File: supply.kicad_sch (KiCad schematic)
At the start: 71 parts, among them Q6 DMG1012T-7, U4 TPS2117DRLR, U5 TPS2117DRLR, U6 PAC1934T_WLCSP, U7 MP5424GRM, U8 MP8869S

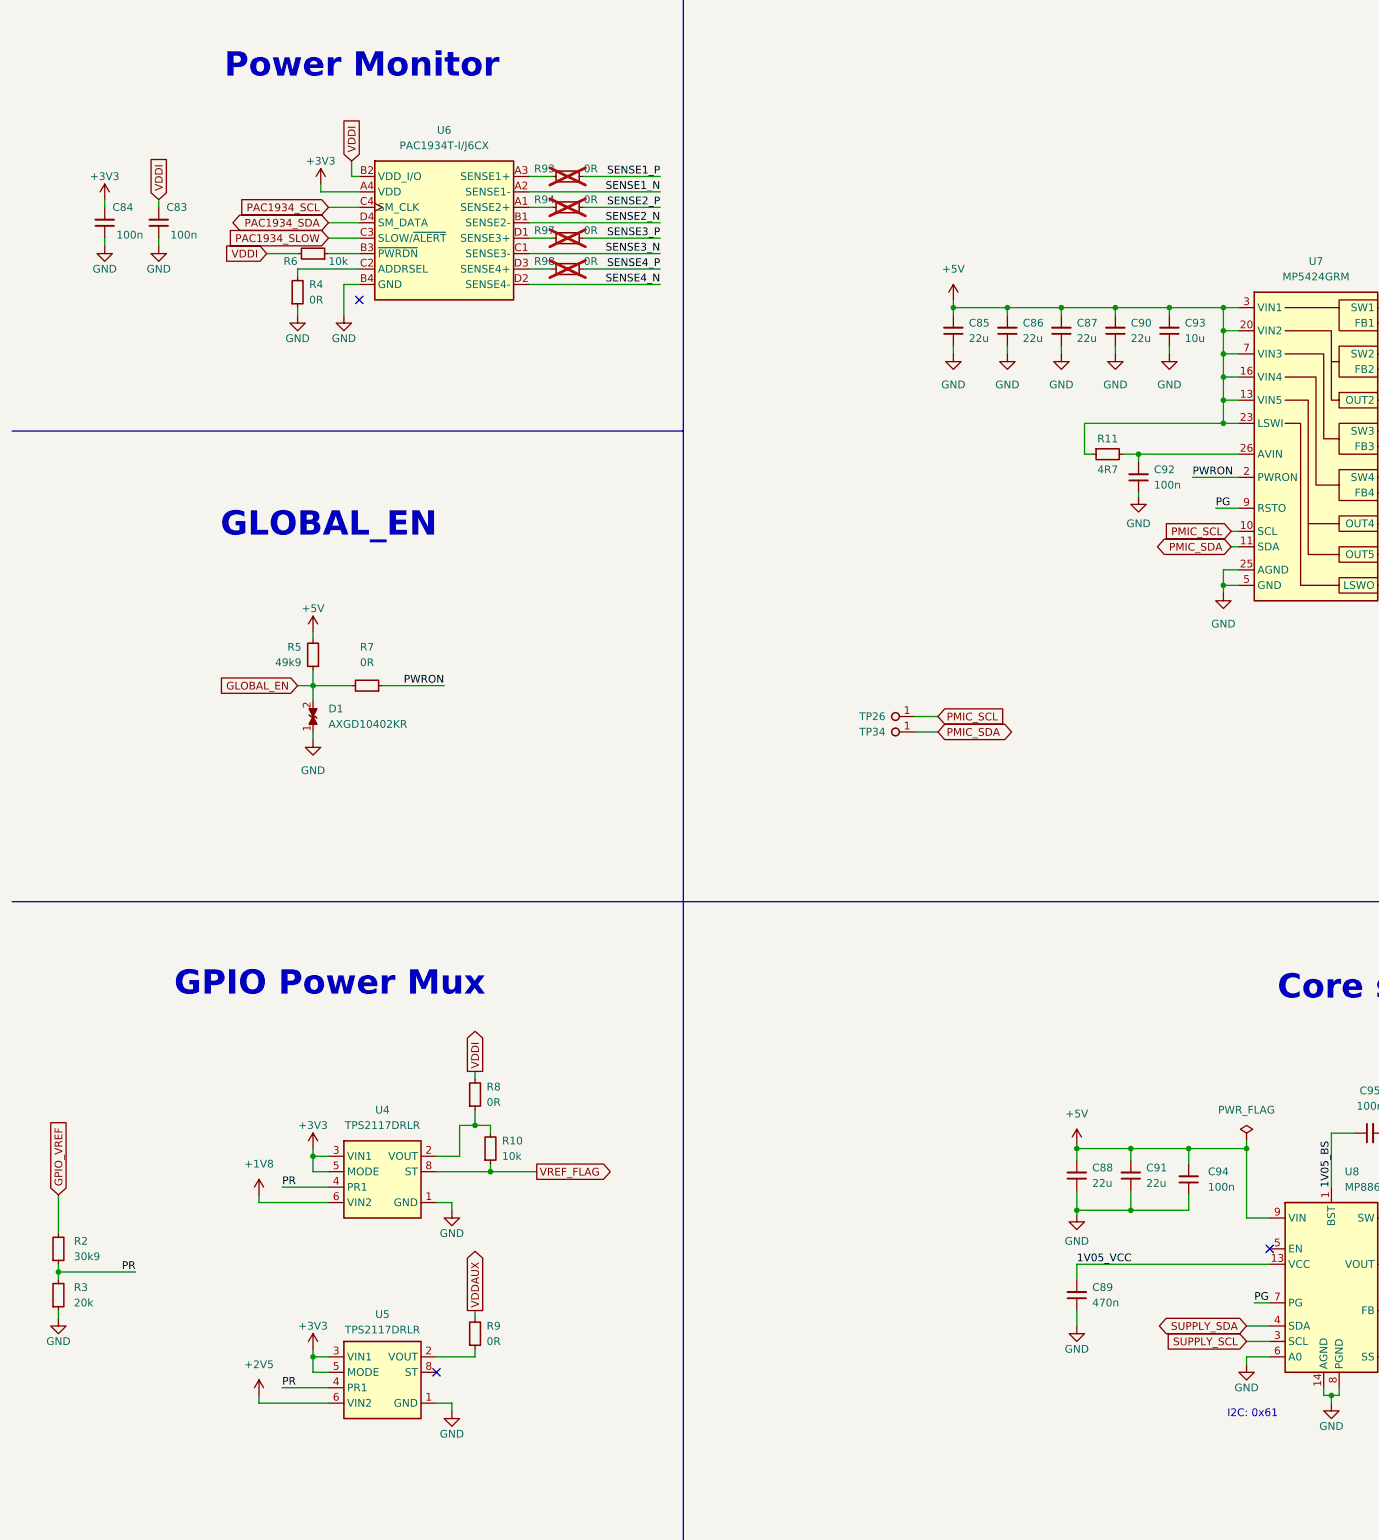
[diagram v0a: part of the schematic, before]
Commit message: [#57505] Continue migration to hierarchical schematic
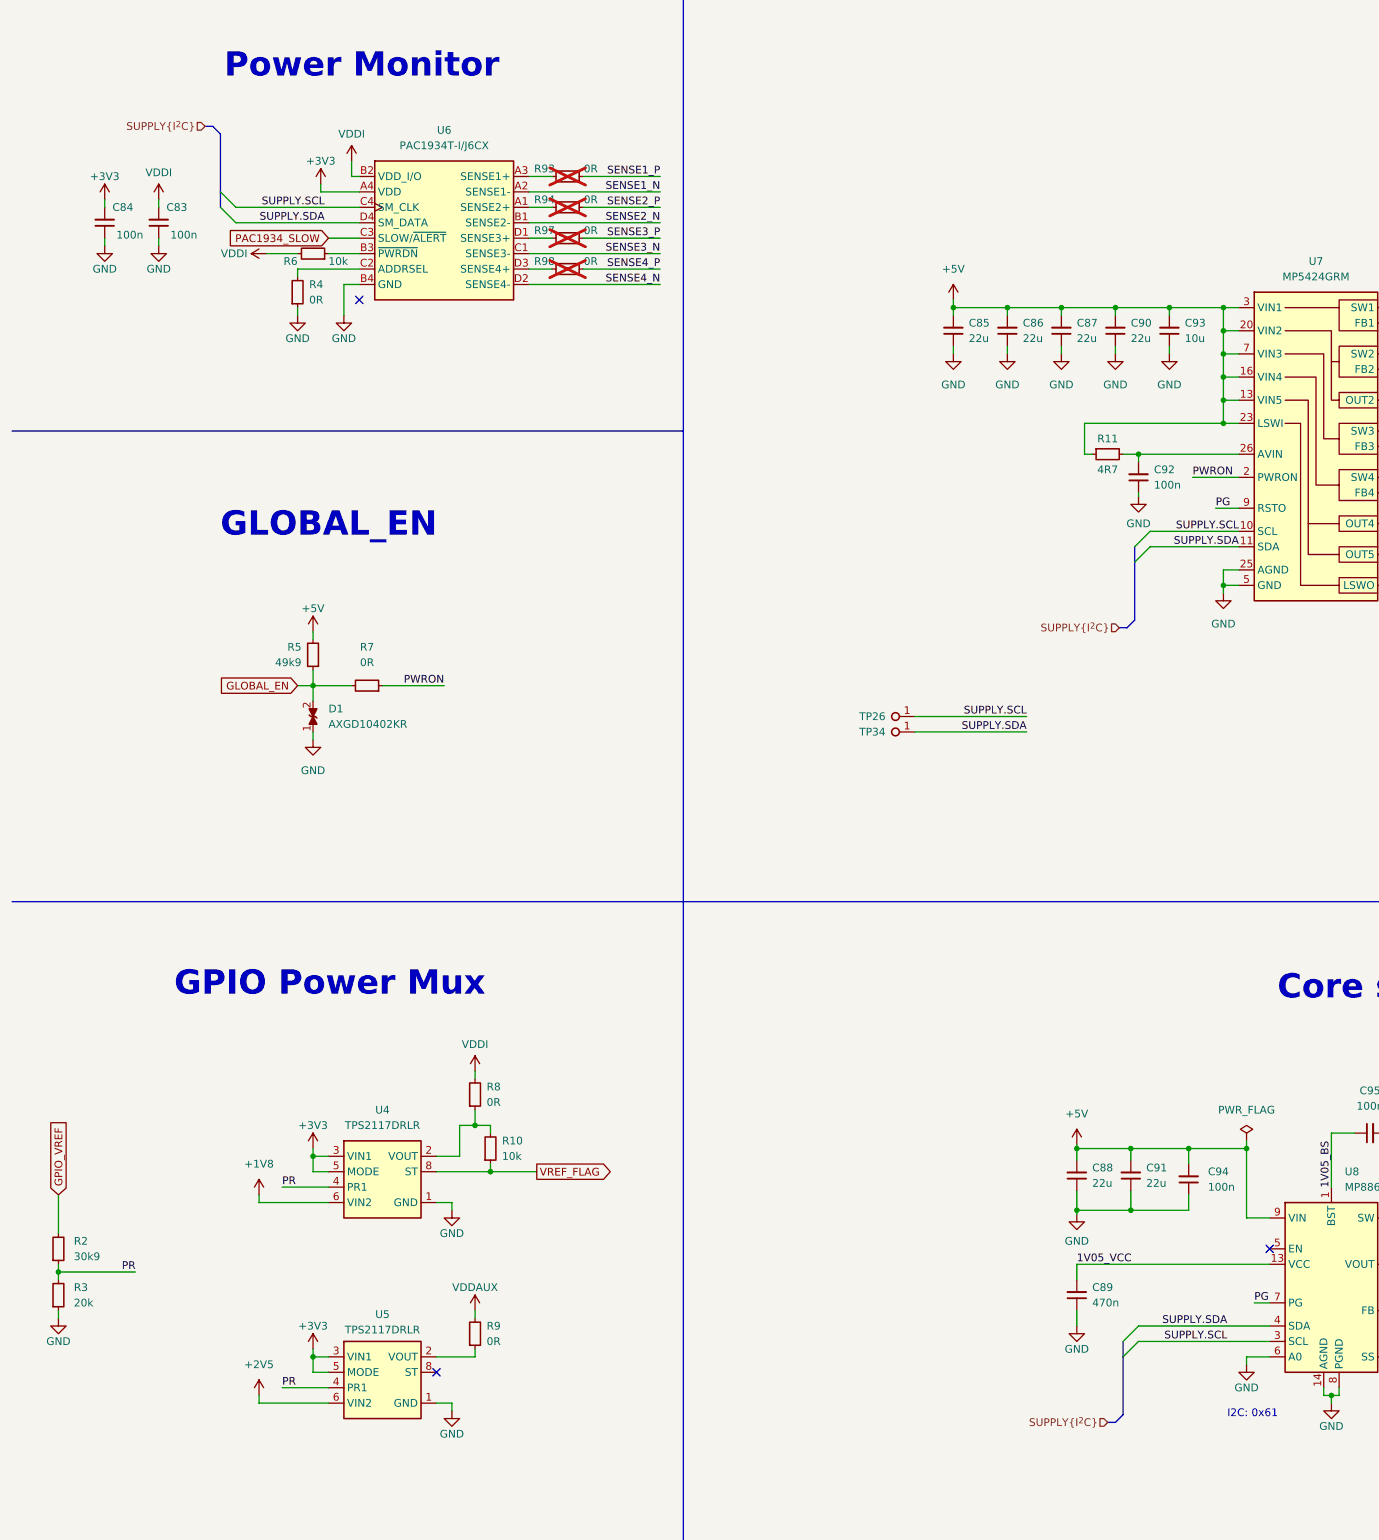
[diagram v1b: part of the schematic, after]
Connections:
- net PMIC_SCL is gone; now on net SUPPLY.SCL: TP26.1, U7.10 (SCL)
- net PMIC_SDA is gone; now on net SUPPLY.SDA: TP34.1, U7.11 (SDA)
- net SUPPLY_SCL is gone; now on net SUPPLY.SCL: U8.3 (SCL)
- net SUPPLY_SDA is gone; now on net SUPPLY.SDA: U8.4 (SDA)
- net PAC1934_SCL renamed SUPPLY.SCL
- net PAC1934_SDA renamed SUPPLY.SDA

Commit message: [#57505] Finish defining buses
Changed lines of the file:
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@@
   (junction (at 259.715 64.77) (diameter 0) (color 0 0 0 0)
   )
-  (junction (at 304.8 222.25) (diameter 0) (color 0 0 0 0)
-  )
   (junction (at 264.16 222.25) (diameter 0) (color 0 0 0 0)
   )
@@
   (junction (at 212.09 80.01) (diameter 0) (color 0 0 0 0)
   )
-  (junction (at 215.9 210.82) (diameter 0) (color 0 0 0 0)
-  )
   (junction (at 274.32 114.3) (diameter 0) (color 0 0 0 0)
   )
@@
     (stroke (width 0) (type default))
   )
-  (wire (pts (xy 215.9 209.55) (xy 215.9 210.82))
-    (stroke (width 0) (type default))
-  )
   (polyline (pts (xy 347.98 91.44) (xy 347.98 109.22))
     (stroke (width 0) (type default))
@@
     (stroke (width 0) (type default))
   )
-  (wire (pts (xy 304.8 222.25) (xy 309.88 222.25))
-    (stroke (width 0) (type default))
-  )
   (polyline (pts (xy 383.54 86.36) (xy 383.54 99.06))
     (stroke (width 0) (type default))
@@
     (stroke (width 0) (type default))
   )
-  (wire (pts (xy 304.8 220.98) (xy 304.8 222.25))
-    (stroke (width 0) (type default))
-  )
   (wire (pts (xy 290.83 64.77) (xy 292.1 64.77))
     (stroke (width 0) (type default))
@@
     (stroke (width 0) (type default))
   )
-  (wire (pts (xy 297.18 222.25) (xy 304.8 222.25))
+  (wire (pts (xy 297.18 222.25) (xy 309.88 222.25))
     (stroke (width 0) (type default))
   )
@@
     )
   )
-  (symbol (lib_id "antmicropower:PWR_FLAG") (at 304.8 220.98 0) (unit 1)
-    (in_bom yes) (on_board yes) (dnp no) (fields_autoplaced)
-    (property "Reference" "#FLG02" (at 304.8 219.075 0)
-      (effects (font (size 1.27 1.27)) hide)
-    )
-    (property "Value" "PWR_FLAG" (at 304.8 215.9 0)
-      (effects (font (size 1.27 1.27)))
-    )
-    (property "Footprint" "" (at 304.8 220.98 0)
-      (effects (font (size 1.27 1.27)) hide)
-    )
-    (property "Datasheet" "" (at 304.8 220.98 0)
-      (effects (font (size 1.27 1.27)) hide)
-    )
-    (pin "1")
-    (instances
-      (project "polarfire-som"
-        (path "/db4a0d3e-2eb3-499e-977d-6eb378cfd3ed/aa0aa716-c477-450b-ad01-6403345c3aae"
-          (reference "#FLG02") (unit 1)
-        )
-      )
-    )
-  )
   (symbol (lib_id "antmicropower:GND") (at 198.12 103.505 0) (unit 1)
     (in_bom yes) (on_board yes) (dnp no)
@@
         )
       )
-    )
-  )
-  (symbol (lib_id "antmicropower:PWR_FLAG") (at 215.9 209.55 0) (unit 1)
-    (in_bom yes) (on_board yes) (dnp no) (fields_autoplaced)
-    (property "Reference" "#FLG01" (at 215.9 207.645 0)
-      (effects (font (size 1.27 1.27)) hide)
-    )
-    (property "Value" "PWR_FLAG" (at 215.9 204.47 0)
-      (effects (font (size 1.27 1.27)))
-    )
-    (property "Footprint" "" (at 215.9 209.55 0)
-      (effects (font (size 1.27 1.27)) hide)
-    )
-    (property "Datasheet" "" (at 215.9 209.55 0)
-      (effects (font (size 1.27 1.27)) hide)
-    )
-    (pin "1")
-    (instances
-      (project "polarfire-som"
-        (path "/db4a0d3e-2eb3-499e-977d-6eb378cfd3ed/aa0aa716-c477-450b-ad01-6403345c3aae"
-          (reference "#FLG01") (unit 1)
-        )
-      )

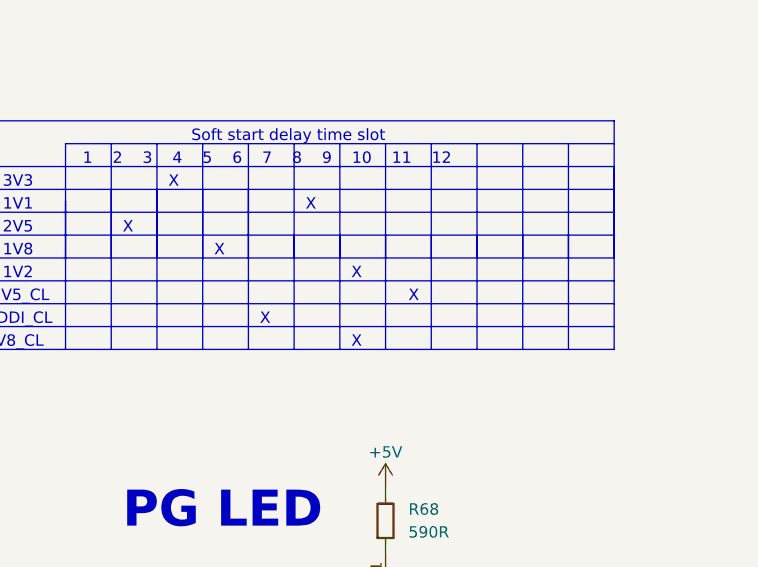
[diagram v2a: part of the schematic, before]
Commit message: [#57422] Update capacitor values
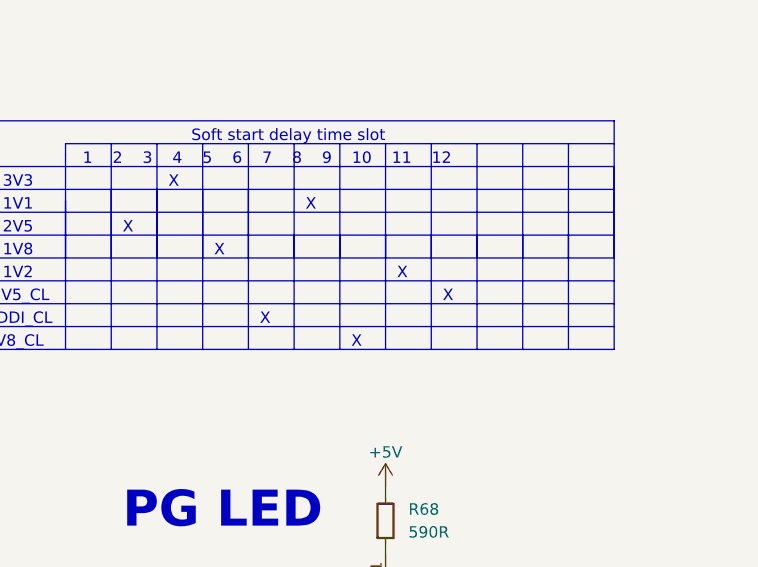
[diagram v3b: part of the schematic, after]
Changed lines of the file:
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@@
     (effects (font (size 1.27 1.27)) (justify left bottom))
   )
-  (text "X" (at 370.84 104.14 0)
+  (text "X" (at 374.65 104.14 0)
     (effects (font (size 1.27 1.27)) (justify left bottom))
   )
@@
     (effects (font (size 1.27 1.27)) (justify left bottom))
   )
-  (text "X" (at 364.49 101.6 0)
+  (text "X" (at 369.57 101.6 0)
     (effects (font (size 1.27 1.27)) (justify left bottom))
   )

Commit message: [#57422] Finishing touches
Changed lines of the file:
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@@
   (title_block
     (title "PolarFire SoM")
-    (date "2024-04-03")
+    (date "2024-04-08")
     (rev "1.0.0")
     (company "Antmicro Ltd")
@@
     (effects (font (size 1.27 1.27)) (justify left bottom))
   )
-  (text "GPIO Power Mux" (at 39.37 186.055 0)
+  (text "GPIO Power Mux" (at 13.97 178.435 0)
     (effects (font (size 4 4) (thickness 0.8) bold) (justify left bottom))
   )
@@
     (effects (font (size 1.27 1.27)) (justify left bottom))
   )
-  (text "Core supply" (at 220.98 186.69 0)
+  (text "Core supply" (at 125.095 179.07 0)
     (effects (font (size 4 4) (thickness 0.8) bold) (justify left bottom))
   )
@@
     (effects (font (size 1.27 1.27)) (justify left bottom))
   )
-  (text "GLOBAL_EN" (at 46.99 110.49 0)
+  (text "GLOBAL_EN" (at 12.7 102.87 0)
     (effects (font (size 4 4) (thickness 0.8) bold) (justify left bottom))
   )
@@
     (effects (font (size 1.27 1.27)) (justify left bottom))
   )
-  (text "Power Monitor" (at 47.625 34.925 0)
+  (text "Power Monitor" (at 13.97 19.685 0)
     (effects (font (size 4 4) (thickness 0.8) bold) (justify left bottom))
   )
@@
     (effects (font (size 1.27 1.27)) (justify left bottom))
   )
-  (text "PMIC" (at 247.65 29.21 0)
+  (text "PMIC" (at 125.095 20.32 0)
     (effects (font (size 4 4) (thickness 0.8) bold) (justify left bottom))
   )

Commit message: [#57422] Align schematics
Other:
- moved on the sheet: C100, C101, C102, C103, C104, C105, C106, C107, C108, C109, C110, C111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

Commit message: [#59446] Add Q5-Q8 to BOM
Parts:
- Q6: now in the parts list
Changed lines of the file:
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@@
   )
   (symbol (lib_id "antmicroTransistorsFETsMOSFETsSingle:DMG1012T-7") (at 359.41 144.78 0) (unit 1)
-    (in_bom no) (on_board yes) (dnp no) (fields_autoplaced)
+    (in_bom yes) (on_board yes) (dnp no) (fields_autoplaced)
     (property "Reference" "Q6" (at 369.57 140.97 0)
       (effects (font (size 1.27 1.27) (thickness 0.15)) (justify left))
